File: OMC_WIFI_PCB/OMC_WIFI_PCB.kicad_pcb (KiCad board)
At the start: 2 copper layers, 103.2 x 83.1 mm, 18 parts, among them J1 ESP32_Left, J10 Control_ACS712, J11 Control_ZMPT101B, J2 ESP32_Right, J3 Power_In, J4 Switch, J5 Pins_FT232R, J6 Line_Relay, J7 Control_Relay, J8 Line_ACS712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

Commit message: Actualización PCB
+ Pista de potencia F. Cu
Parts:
- moved REF** 24.0 mm to (635.0, -953.6)
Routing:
- net NEUTRAL: track 69.7 -> 139.4 mm
- net LINE: track 44.0 -> 88.1 mm
- net NO: track 20.7 -> 41.4 mm
- net Net-(F1-Pad1): track 18.2 -> 36.4 mm
- net COM: track 14.7 -> 29.3 mm

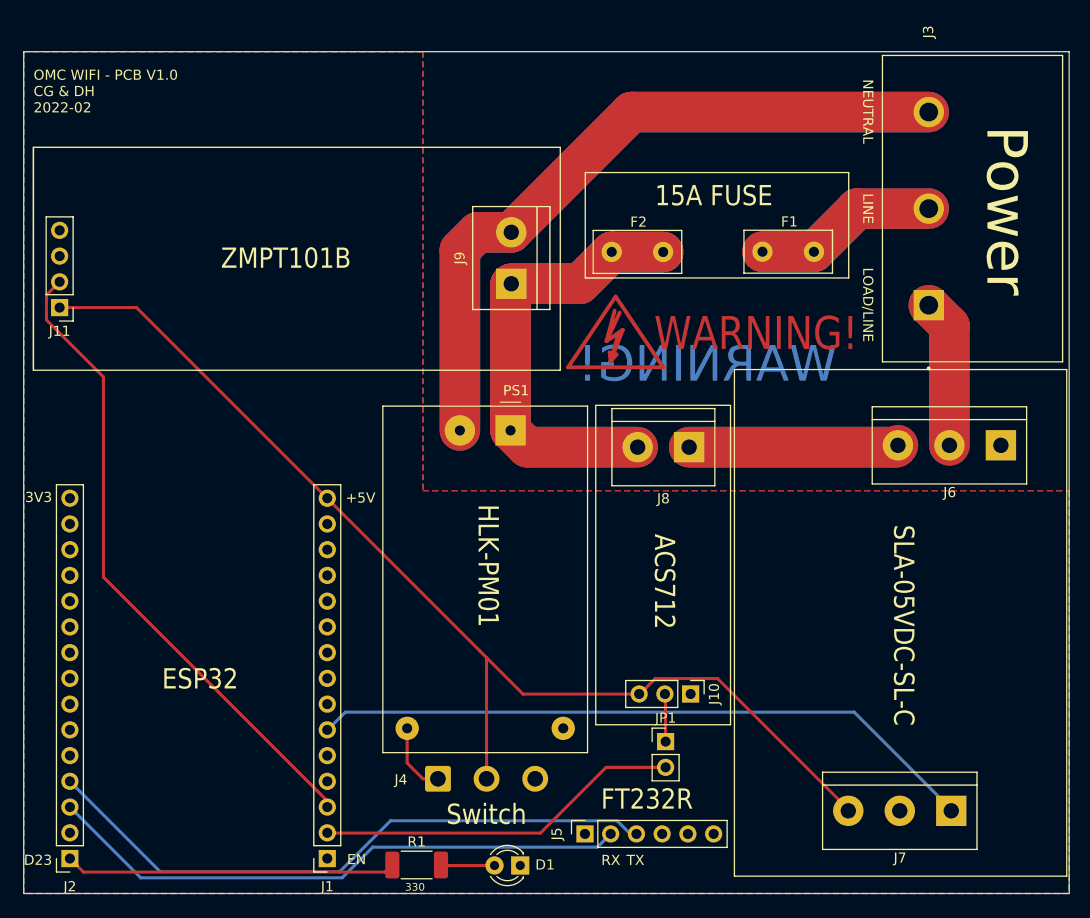
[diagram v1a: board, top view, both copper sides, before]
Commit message: Actualización PCB
> Divisores de tensión
> Nuevos Gerbers
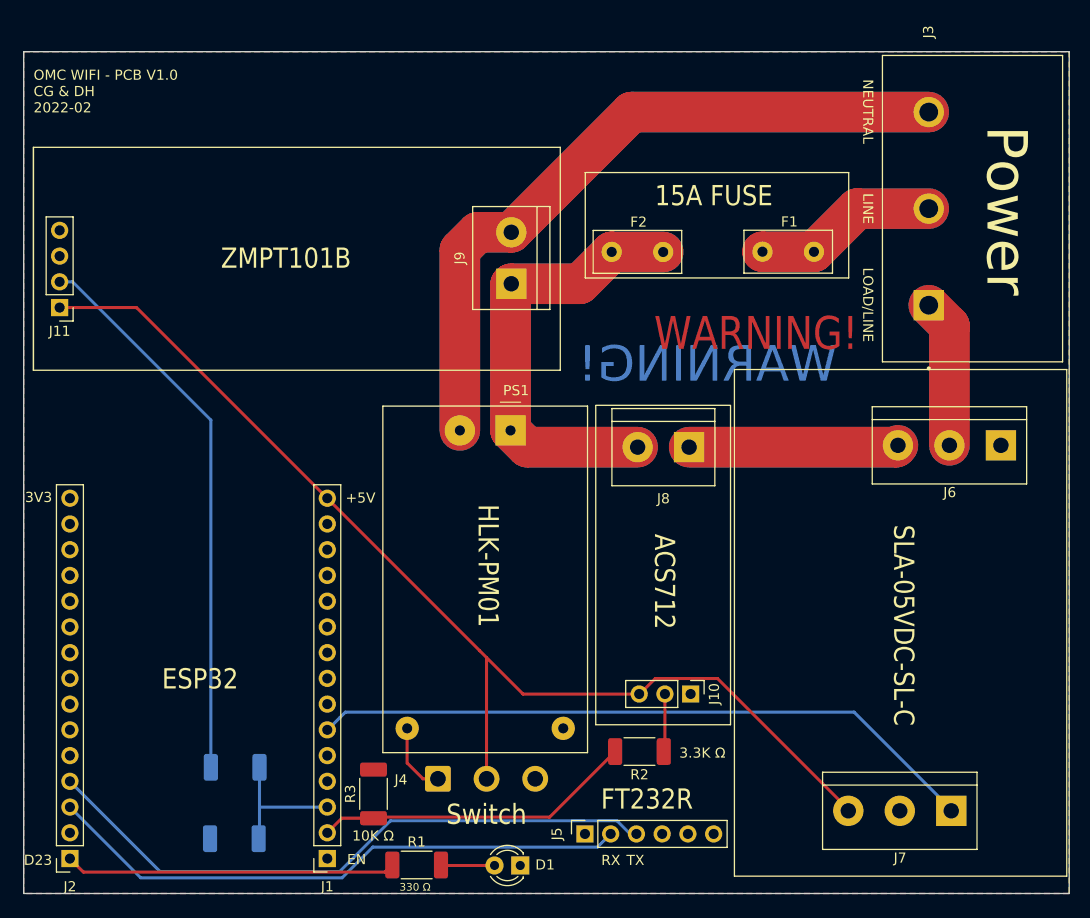
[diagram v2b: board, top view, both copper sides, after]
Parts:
- removed JP1: Jumper, Connector_PinHeader_2.54mm:PinHeader_1x02_P2.54mm_Vertical
- removed REF**: Symbol_HighVoltage_Type2_CopperTop_VerySmall, Symbol:Symbol_HighVoltage_Type2_CopperTop_VerySmall
- added R2: 3.3K, Resistor_SMD:R_2010_5025Metric_Pad1.40x2.65mm_HandSolder, F.Cu at (637.4, -912.9)
- added R3: 10K, Resistor_SMD:R_2010_5025Metric_Pad1.40x2.65mm_HandSolder, F.Cu at (611.1, -908.7)
- added R4: 3.3K, Resistor_SMD:R_2010_5025Metric_Pad1.40x2.65mm_HandSolder, B.Cu at (597.5, -911.3)
- added R5: 10K, Resistor_SMD:R_2010_5025Metric_Pad1.40x2.65mm_HandSolder, B.Cu at (597.4, -904.3)
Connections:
- J11 pad 2: VN_ZMPT -> Net-(J11-Pad2)
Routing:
- net Net-(J11-Pad2): track 0.00 -> 54.8 mm
- net VN_ZMPT: track 63.9 -> 14.4 mm
- net VP_ACS: track 36.1 -> 31.7 mm
- net Net-(J10-Pad2): track 4.69 -> 5.73 mm
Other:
- board text added: "10K Ω"
- board text added: "3.3K Ω"
- board text added: "330 Ω"
- board text removed: "330"
